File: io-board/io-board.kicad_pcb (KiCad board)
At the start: 2 copper layers, 82 x 64 mm, 65 parts, among them J1 Conn_01x03, J2 Conn_01x03, J3 Conn_01x03, J4 Conn_01x03, J5 Conn_01x24, K1 FRM18A-5 DC12V, K10 FRM18A-5 DC12V, K11 FRM18A-5 DC12V, K2 FRM18A-5 DC12V, K3 FRM18A-5 DC12V, K4 FRM18A-5 DC12V, K5 FRM18A-5 DC12V, K6 FRM18A-5 DC12V, K7 FRM18A-5 DC12V, K8 FRM18A-5 DC12V, K9 FRM18A-5 DC12V, Q1 NPN, Q10 NPN, Q11 NPN, Q2 NPN, Q3 NPN, Q4 NPN, Q5 NPN, Q6 NPN, Q7 NPN, Q8 NPN, Q9 NPN

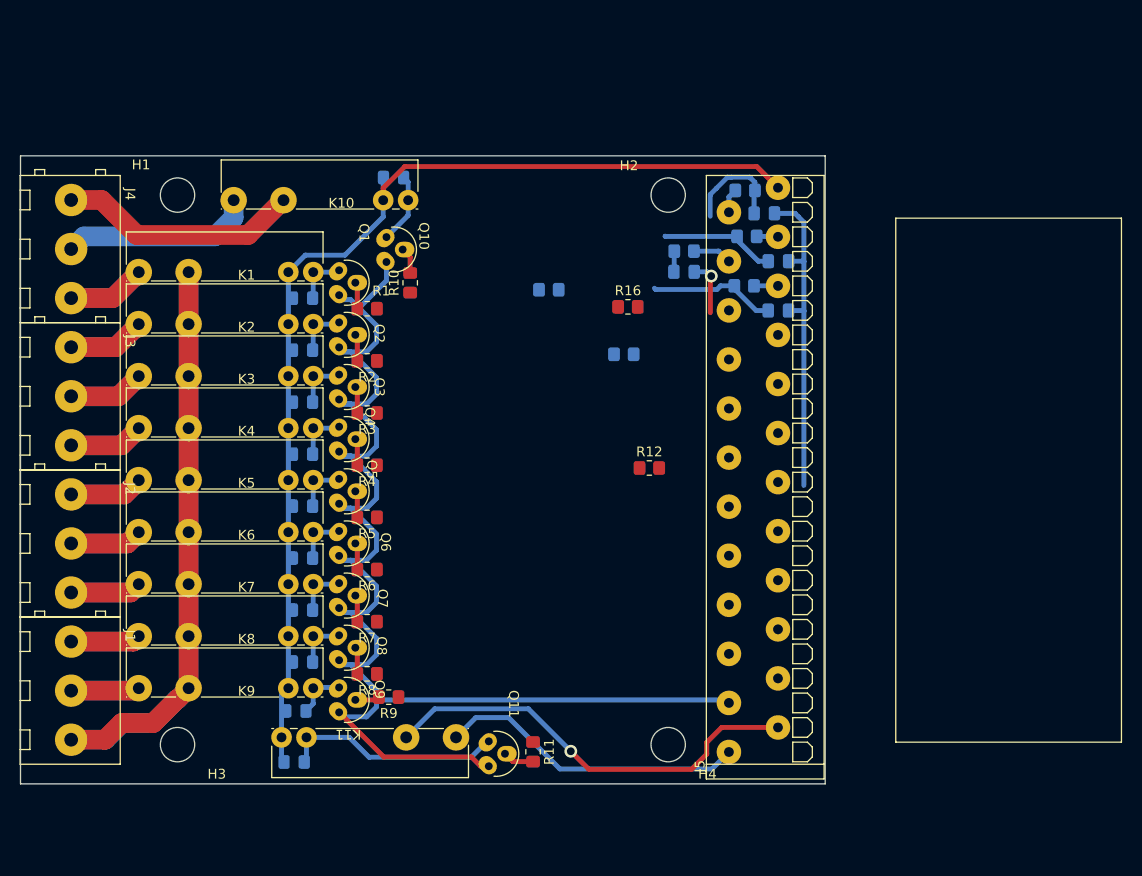
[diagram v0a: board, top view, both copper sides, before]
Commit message: Add STM32 module
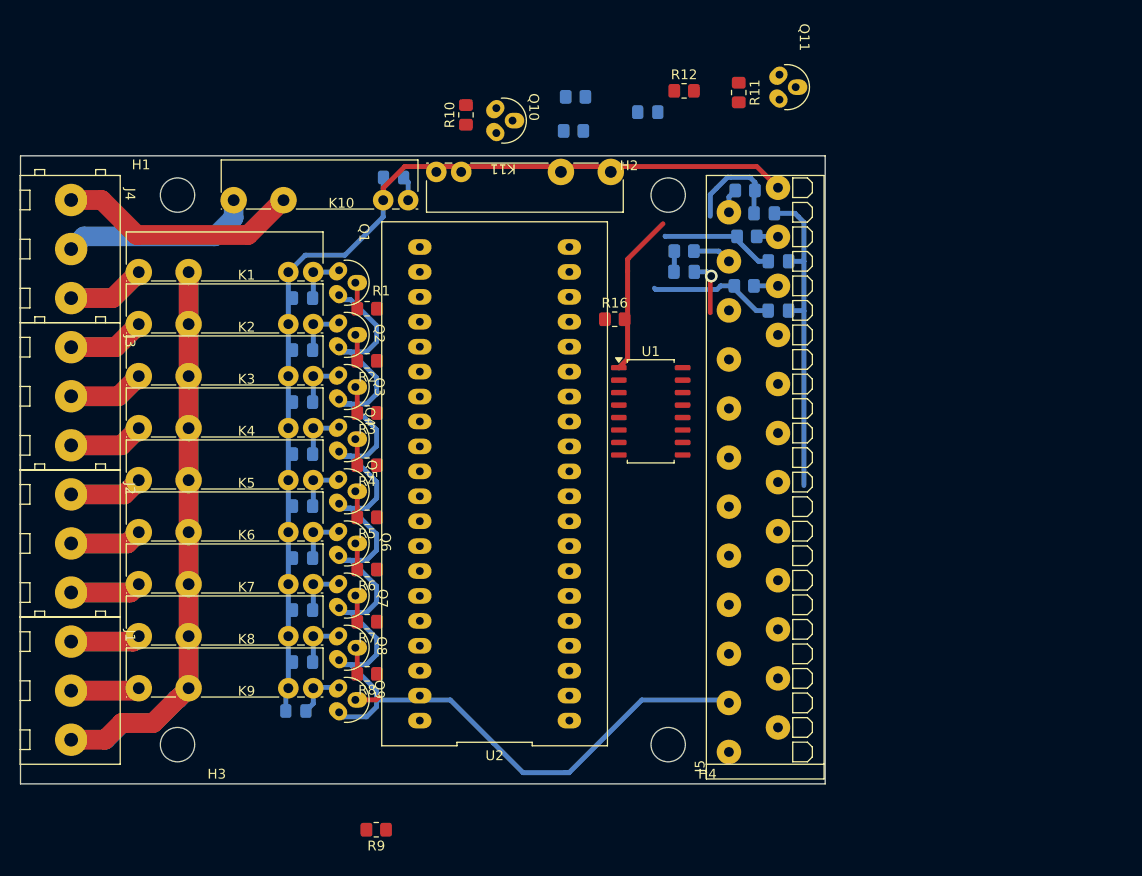
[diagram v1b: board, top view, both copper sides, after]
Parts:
- added U1: Littelfuse SP720, Package_SO:SOIC-16_4.55x10.3mm_P1.27mm, F.Cu at (94.2, 56.0)
- added U2: Kamod BluePill STM32F103C8T6, Footprints:Kamod-BluePill-STM32F103C8T6, F.Cu at (78.3, 63.4)
- moved D11 75.4 mm to (93.9, 25.6)
- moved Q11 74.1 mm to (107.3, 21.7)
- moved R11 70.4 mm to (103.2, 23.6)
- moved K11 59.7 mm to (72.4, 31.6)
- moved R12 38.6 mm to (97.6, 23.4)
- moved R14 23.3 mm to (86.3, 27.5)
- moved R18 19.8 mm to (86.6, 24.0)
- moved R10 18.0 mm to (75.4, 25.8)
- moved Q10 17.3 mm to (78.5, 25.1)
- moved R9 13.6 mm to (66.2, 98.7)
- moved R16 1.85 mm to (90.5, 46.6)
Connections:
- J1 pad 1: /REL8-OUT -> /Relays/REL8-OUT
- J1 pad 2: /REL9-OUT -> /Relays/REL9-OUT
- J1 pad 3: /REL-COM -> /Relays/REL-COM
- J2 pad 1: /REL5-OUT -> /Relays/REL5-OUT
- J2 pad 2: /REL6-OUT -> /Relays/REL6-OUT
- J2 pad 3: /REL7-OUT -> /Relays/REL7-OUT
- J3 pad 1: /REL2-OUT -> /Relays/REL2-OUT
- J3 pad 2: /REL3-OUT -> /Relays/REL3-OUT
- J3 pad 3: /REL4-OUT -> /Relays/REL4-OUT
- J4 pad 1: /REL10-OUT1 -> /Relays/REL10-OUT1
- J4 pad 2: /REL10-OUT2 -> /Relays/REL10-OUT2
- J4 pad 3: /REL1-OUT -> /Relays/REL1-OUT
- J5 pad 1: /REL11-OUT1 -> REL11-OUT1
- J5 pad 2: /REL11-OUT2 -> REL11-OUT2
- K11 pad 13: /Relays/REL11-OUT2 -> REL11-OUT2
- K11 pad 14: /Relays/REL11-OUT1 -> REL11-OUT1
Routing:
- net /Relays/REL-COM: track 0.00 -> 112.9 mm
- net /REL-COM: track 112.9 -> 0.00 mm
- net /REL11-OUT2: track 44.1 -> 0.00 mm, vias 1 -> 0
- net /REL11-OUT1: track 31.5 -> 0.00 mm
- net /Relays/REL10-OUT1: track 0.00 -> 24.6 mm
- net /REL10-OUT1: track 24.6 -> 0.00 mm
- net Net-(D11-A): track 22.5 -> 0.00 mm
- net /Relays/REL10-OUT2: track 0.00 -> 19.7 mm
- net /REL10-OUT2: track 19.7 -> 0.00 mm
- net GND: track 182.8 -> 165.5 mm
- net /ESD1: track 10.9 -> 27.4 mm
- net /Relays/REL1-OUT: track 0.00 -> 16.0 mm
- net /REL1-OUT: track 16.0 -> 0.00 mm
- net /Relays/REL2-OUT: track 0.00 -> 15.7 mm
- net /REL2-OUT: track 15.7 -> 0.00 mm
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
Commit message: Almost all connected except OC and LED drivers
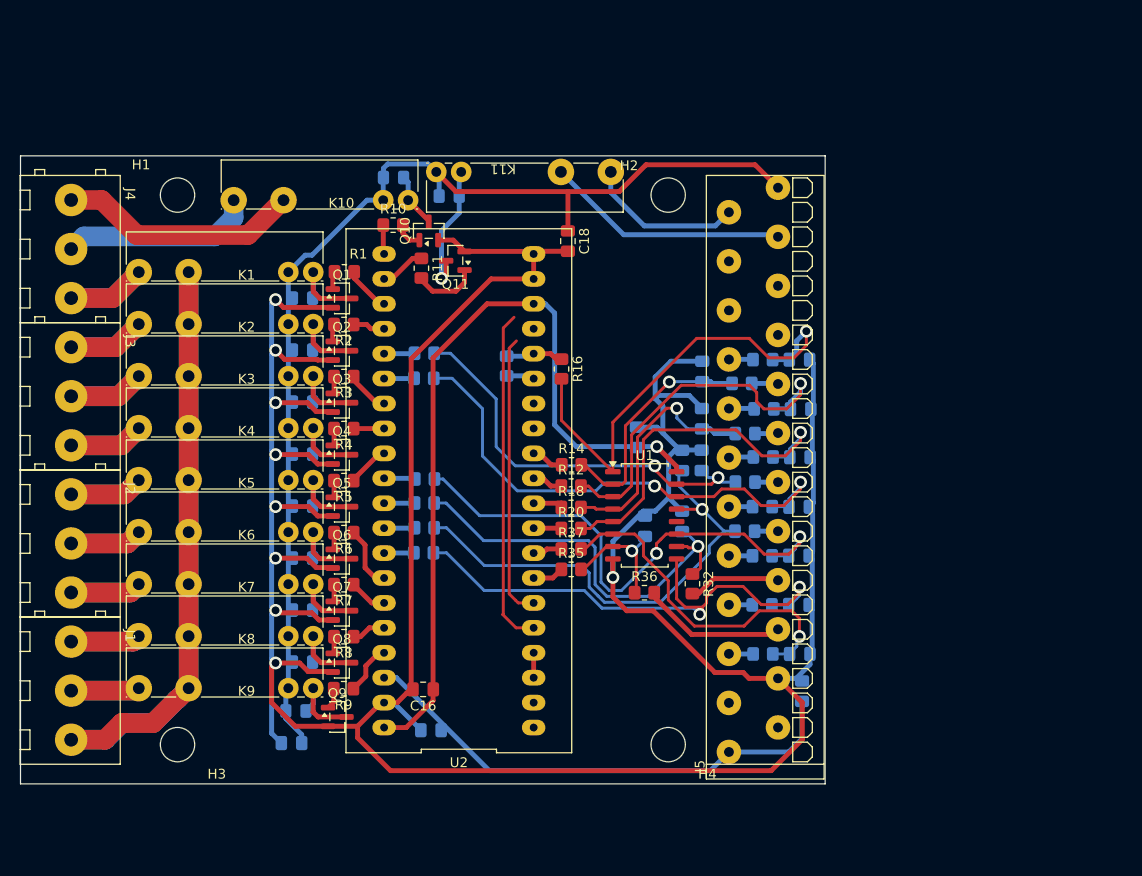
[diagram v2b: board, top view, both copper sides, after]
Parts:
- added C10: C, Capacitor_SMD:C_0805_2012Metric_Pad1.18x1.45mm_HandSolder, B.Cu at (97.4, 67.2)
- added C11: C, Capacitor_SMD:C_0805_2012Metric_Pad1.18x1.45mm_HandSolder, B.Cu at (109.3, 75.8)
- added C12: C, Capacitor_SMD:C_0805_2012Metric_Pad1.18x1.45mm_HandSolder, B.Cu at (93.6, 67.8)
- added C13: C, Capacitor_SMD:C_0805_2012Metric_Pad1.18x1.45mm_HandSolder, B.Cu at (109.4, 80.8)
- added C14: C, Capacitor_SMD:C_0805_2012Metric_Pad1.18x1.45mm_HandSolder, B.Cu at (92.8, 58.7)
- added C15: C, Capacitor_SMD:C_0805_2012Metric_Pad1.18x1.45mm_HandSolder, B.Cu at (71.8, 88.5)
- added C16: C, Capacitor_SMD:C_0805_2012Metric_Pad1.18x1.45mm_HandSolder, F.Cu at (71.0, 84.4)
- added C17: C, Capacitor_SMD:C_0805_2012Metric_Pad1.18x1.45mm_HandSolder, B.Cu at (109.6, 84.5)
- added C18: C, Capacitor_SMD:C_0805_2012Metric_Pad1.18x1.45mm_HandSolder, F.Cu at (85.8, 38.7)
- added C19: C, Capacitor_SMD:C_0805_2012Metric_Pad1.18x1.45mm_HandSolder, B.Cu at (57.6, 89.8)
- added C5: C, Capacitor_SMD:C_0805_2012Metric_Pad1.18x1.45mm_HandSolder, B.Cu at (109.4, 60.7)
- added C6: C, Capacitor_SMD:C_0805_2012Metric_Pad1.18x1.45mm_HandSolder, B.Cu at (99.4, 61.0)
- added C7: C, Capacitor_SMD:C_0805_2012Metric_Pad1.18x1.45mm_HandSolder, B.Cu at (109.3, 65.8)
- added C8: C, Capacitor_SMD:C_0805_2012Metric_Pad1.18x1.45mm_HandSolder, B.Cu at (97.4, 61.0)
- added C9: C, Capacitor_SMD:C_0805_2012Metric_Pad1.18x1.45mm_HandSolder, B.Cu at (109.3, 70.7)
- added R20: R, Resistor_SMD:R_0805_2012Metric_Pad1.20x1.40mm_HandSolder, F.Cu at (86.1, 68.0)
- added R21: R, Resistor_SMD:R_0805_2012Metric_Pad1.20x1.40mm_HandSolder, B.Cu at (105.7, 60.7)
- added R22: R, Resistor_SMD:R_0805_2012Metric_Pad1.20x1.40mm_HandSolder, B.Cu at (79.5, 51.4)
- added R23: R, Resistor_SMD:R_0805_2012Metric_Pad1.20x1.40mm_HandSolder, B.Cu at (71.2, 50.1)
- added R24: R, Resistor_SMD:R_0805_2012Metric_Pad1.20x1.40mm_HandSolder, B.Cu at (103.8, 63.2)
- added R25: R, Resistor_SMD:R_0805_2012Metric_Pad1.20x1.40mm_HandSolder, B.Cu at (71.1, 52.7)
- added R26: R, Resistor_SMD:R_0805_2012Metric_Pad1.20x1.40mm_HandSolder, B.Cu at (105.6, 65.8)
- added R27: R, Resistor_SMD:R_0805_2012Metric_Pad1.20x1.40mm_HandSolder, B.Cu at (71.2, 67.9)
- added R28: R, Resistor_SMD:R_0805_2012Metric_Pad1.20x1.40mm_HandSolder, B.Cu at (103.8, 68.2)
- added R29: R, Resistor_SMD:R_0805_2012Metric_Pad1.20x1.40mm_HandSolder, B.Cu at (71.2, 62.9)
- added R30: R, Resistor_SMD:R_0805_2012Metric_Pad1.20x1.40mm_HandSolder, B.Cu at (105.6, 70.8)
- added R31: R, Resistor_SMD:R_0805_2012Metric_Pad1.20x1.40mm_HandSolder, B.Cu at (71.2, 65.4)
- added R32: R, Resistor_SMD:R_0805_2012Metric_Pad1.20x1.40mm_HandSolder, F.Cu at (98.5, 73.6)
- added R33: R, Resistor_SMD:R_0805_2012Metric_Pad1.20x1.40mm_HandSolder, B.Cu at (71.1, 70.5)
- added R34: R, Resistor_SMD:R_0805_2012Metric_Pad1.20x1.40mm_HandSolder, B.Cu at (105.6, 75.8)
- added R35: R, Resistor_SMD:R_0805_2012Metric_Pad1.20x1.40mm_HandSolder, F.Cu at (86.1, 72.1)
- added R36: R, Resistor_SMD:R_0805_2012Metric_Pad1.20x1.40mm_HandSolder, F.Cu at (93.6, 74.5)
- added R37: R, Resistor_SMD:R_0805_2012Metric_Pad1.20x1.40mm_HandSolder, F.Cu at (86.1, 70.1)
- added R38: R, Resistor_SMD:R_0805_2012Metric_Pad1.20x1.40mm_HandSolder, B.Cu at (105.7, 80.8)
- Q1, Q10, Q11, Q2, Q3, Q4, Q5, Q6, Q7, Q8, Q9: footprint Footprints:TO-92-3 -> Package_TO_SOT_SMD:SOT-23
- R14, R18: moved to F.Cu
- moved R12 41.9 mm to (86.1, 63.6)
- moved R18 41.8 mm to (86.1, 65.8)
- moved Q11 38.1 mm to (74.3, 40.7), turned to 180 degrees
- moved R11 37.0 mm to (70.8, 41.5)
- moved R14 34.0 mm to (86.2, 61.5), turned to 0 degrees
- moved D11 22.0 mm to (73.7, 34.1)
- moved C3 18.4 mm to (109.5, 55.8)
- moved R13 18.0 mm to (105.8, 55.8), turned to 180 degrees
- moved R17 17.3 mm to (105.6, 50.8)
- moved C1 15.3 mm to (109.4, 50.8)
- moved R19 15.1 mm to (103.8, 58.3)
- moved R15 15.0 mm to (103.5, 53.2)
- moved R9 14.8 mm to (62.9, 84.3)
- moved Q10 14.3 mm to (71.6, 37.6), turned to 90 degrees
- moved C2 13.7 mm to (99.5, 52.0), turned to 90 degrees
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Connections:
- J5 pad 1: REL11-OUT1 -> +5V
- J5 pad 10: /OC1 -> /IO7
- J5 pad 11: /OC2 -> /IO6
- J5 pad 12: /IO12 -> /IO5
- J5 pad 13: /IO11 -> /IO4
- J5 pad 14: /IO10 -> /IO3
- J5 pad 15: /IO9 -> /IO2
- J5 pad 16: /IO8 -> /IO1
- J5 pad 17: /IO7 -> /UART
- J5 pad 18: /IO6 -> /LED1-P
- J5 pad 19: /IO5 -> /LED1-M
- J5 pad 2: REL11-OUT2 -> /OC1
- J5 pad 20: /IO4 -> /LED2-P
- J5 pad 21: /IO3 -> /LED2-M
- J5 pad 22: /IO2 -> REL11-OUT2
- J5 pad 23: /IO1 -> REL11-OUT1
- J5 pad 3: GND -> /OC2
- J5 pad 4: +5V -> GND
- J5 pad 5: /UART -> /IO12
- J5 pad 6: /LED1-P -> /IO11
- J5 pad 7: /LED1-M -> /IO10
- J5 pad 8: /LED2-P -> /IO9
- J5 pad 9: /LED2-M -> /IO8
- Q1 pad 1: Net-(D1-A) -> Net-(Q1-B)
- Q1 pad 2: Net-(Q1-B) -> GND
- Q1 pad 3: GND -> Net-(D1-A)
- Q10 pad 1: Net-(D10-A) -> Net-(Q10-B)
- Q10 pad 2: Net-(Q10-B) -> GND
- Q10 pad 3: GND -> Net-(D10-A)
- Q11 pad 1: Net-(D11-A) -> Net-(Q11-B)
- Q11 pad 2: Net-(Q11-B) -> GND
- Q11 pad 3: GND -> Net-(D11-A)
- Q2 pad 1: Net-(D2-A) -> Net-(Q2-B)
- Q2 pad 2: Net-(Q2-B) -> GND
- Q2 pad 3: GND -> Net-(D2-A)
- Q3 pad 1: Net-(D3-A) -> Net-(Q3-B)
- Q3 pad 2: Net-(Q3-B) -> GND
- Q3 pad 3: GND -> Net-(D3-A)
- Q4 pad 1: Net-(D4-A) -> Net-(Q4-B)
- Q4 pad 2: Net-(Q4-B) -> GND
- Q4 pad 3: GND -> Net-(D4-A)
- Q5 pad 1: Net-(D5-A) -> Net-(Q5-B)
- Q5 pad 2: Net-(Q5-B) -> GND
- Q5 pad 3: GND -> Net-(D5-A)
- Q6 pad 1: Net-(D6-A) -> Net-(Q6-B)
- Q6 pad 2: Net-(Q6-B) -> GND
- Q6 pad 3: GND -> Net-(D6-A)
- Q7 pad 1: Net-(D7-A) -> Net-(Q7-B)
- Q7 pad 2: Net-(Q7-B) -> GND
- Q7 pad 3: GND -> Net-(D7-A)
- Q8 pad 1: Net-(D8-A) -> Net-(Q8-B)
- Q8 pad 2: Net-(Q8-B) -> GND
- Q8 pad 3: GND -> Net-(D8-A)
- Q9 pad 1: Net-(D9-A) -> Net-(Q9-B)
- Q9 pad 2: Net-(Q9-B) -> GND
- Q9 pad 3: GND -> Net-(D9-A)
- R1 pad 1: /Relays/REL1-IN -> REL1-IN
- R10 pad 1: /Relays/REL10-IN -> REL10-IN
- R11 pad 1: /Relays/REL11-IN -> REL11-IN
- R12 pad 1: /IO3/IO-IN -> /IO-IN2
- R13 pad 2: /IO3 -> /IO2
- R14 pad 1: /IO2/IO-IN -> /IO-IN1
- R15 pad 2: /IO2 -> /IO1
- R16 pad 1: /IO1/IO-IN -> RXD
- R17 pad 2: /IO1 -> /UART
- R18 pad 1: /IO4/IO-IN -> /IO-IN3
- R19 pad 2: /IO4 -> /IO3
- R2 pad 1: /Relays/REL2-IN -> REL2-IN
- R3 pad 1: /Relays/REL3-IN -> REL3-IN
- R4 pad 1: /Relays/REL4-IN -> REL4-IN
- R5 pad 1: /Relays/REL5-IN -> REL5-IN
- R6 pad 1: /Relays/REL6-IN -> REL6-IN
- R7 pad 1: /Relays/REL7-IN -> REL7-IN
- R8 pad 1: /Relays/REL8-IN -> REL8-IN
- R9 pad 1: /Relays/REL9-IN -> REL9-IN
- U1 pad 10: unconnected-(U1-Pin_10-Pad10) -> /ESD9
- U1 pad 11: unconnected-(U1-Pin_11-Pad11) -> /ESD10
- U1 pad 12: unconnected-(U1-Pin_12-Pad12) -> /ESD11
- U1 pad 13: unconnected-(U1-Pin_13-Pad13) -> /ESD12
- U1 pad 14: unconnected-(U1-Pin_14-Pad14) -> /ESD13
- U1 pad 15: unconnected-(U1-Pin_15-Pad15) -> /ESD14
- U1 pad 5: unconnected-(U1-Pin_5-Pad5) -> /ESD5
- U1 pad 6: unconnected-(U1-Pin_6-Pad6) -> /ESD6
- U1 pad 7: unconnected-(U1-Pin_7-Pad7) -> /ESD7
- U1 pad 9: unconnected-(U1-Pin_9-Pad9) -> /ESD8
- U2 pad 10: unconnected-(U2-Pin_10-Pad10) -> /IO-IN3
- U2 pad 11: unconnected-(U2-Pin_11-Pad11) -> /IO-IN2
- U2 pad 12: unconnected-(U2-Pin_12-Pad12) -> /IO-IN1
- U2 pad 15: unconnected-(U2-Pin_15-Pad15) -> TXD
- U2 pad 16: unconnected-(U2-Pin_16-Pad16) -> RXD
- U2 pad 21: unconnected-(U2-Pin_21-Pad21) -> REL10-IN
- U2 pad 22: unconnected-(U2-Pin_22-Pad22) -> REL11-IN
- U2 pad 23: unconnected-(U2-Pin_23-Pad23) -> REL1-IN
- U2 pad 24: unconnected-(U2-Pin_24-Pad24) -> REL2-IN
- U2 pad 25: unconnected-(U2-Pin_25-Pad25) -> /IO-IN5
- U2 pad 26: unconnected-(U2-Pin_26-Pad26) -> /IO-IN6
- U2 pad 27: unconnected-(U2-Pin_27-Pad27) -> REL3-IN
- U2 pad 28: unconnected-(U2-Pin_28-Pad28) -> REL4-IN
- U2 pad 29: unconnected-(U2-Pin_29-Pad29) -> REL5-IN
- U2 pad 3: unconnected-(U2-Pin_3-Pad3) -> Net-(U2-Pin_3)
- U2 pad 30: unconnected-(U2-Pin_30-Pad30) -> /IO-IN8
- U2 pad 31: unconnected-(U2-Pin_31-Pad31) -> /IO-IN9
- U2 pad 32: unconnected-(U2-Pin_32-Pad32) -> /IO-IN7
- U2 pad 33: unconnected-(U2-Pin_33-Pad33) -> /IO-IN10
- U2 pad 34: unconnected-(U2-Pin_34-Pad34) -> REL6-IN
- U2 pad 35: unconnected-(U2-Pin_35-Pad35) -> REL7-IN
- U2 pad 36: unconnected-(U2-Pin_36-Pad36) -> REL8-IN
- U2 pad 37: unconnected-(U2-Pin_37-Pad37) -> REL9-IN
- U2 pad 4: unconnected-(U2-Pin_4-Pad4) -> Net-(U2-Pin_3)
- U2 pad 5: unconnected-(U2-Pin_5-Pad5) -> /LED1-PWM
- U2 pad 6: unconnected-(U2-Pin_6-Pad6) -> /LED2-PWM
- U2 pad 7: unconnected-(U2-Pin_7-Pad7) -> /IO-IN11
- U2 pad 8: unconnected-(U2-Pin_8-Pad8) -> /IO-IN12
- U2 pad 9: unconnected-(U2-Pin_9-Pad9) -> /IO-IN4
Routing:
- net GND: track 165.5 -> 350.6 mm, vias 1 -> 9
- net +3.3V: track 0.00 -> 82.2 mm, vias 0 -> 1
- net /ESD8: track 0.00 -> 54.8 mm, vias 0 -> 2
- net /ESD10: track 0.00 -> 53.9 mm, vias 0 -> 2
- net /ESD13: track 0.00 -> 53.0 mm, vias 0 -> 2
- net +5V: track 0.00 -> 51.7 mm
- net /ESD12: track 0.00 -> 48.8 mm, vias 0 -> 1
- net /ESD9: track 0.00 -> 43.4 mm, vias 0 -> 1
- net /ESD14: track 0.00 -> 41.4 mm, vias 0 -> 2
- net /ESD5: track 0.00 -> 37.3 mm, vias 0 -> 1
- net /ESD3: track 2.13 -> 38.6 mm, vias 0 -> 1
- net /ESD6: track 0.00 -> 35.4 mm, vias 0 -> 1
- net /LED1-PWM: track 0.00 -> 34.5 mm
- net /LED2-PWM: track 0.00 -> 29.0 mm
- net REL11-OUT2: track 0.00 -> 24.9 mm
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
